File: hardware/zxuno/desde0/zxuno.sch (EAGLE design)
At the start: 98 parts, among them J1 microUSB, J12 AUX_PW, J13 SWITCH, J14 RESET_FPGA, J4 Audio, J5 EAR, J7 MINI-DIN6PTH, T1 BC846, U1 6SLX9TQG144, U2 FLASH-SPI-25XXSMD1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

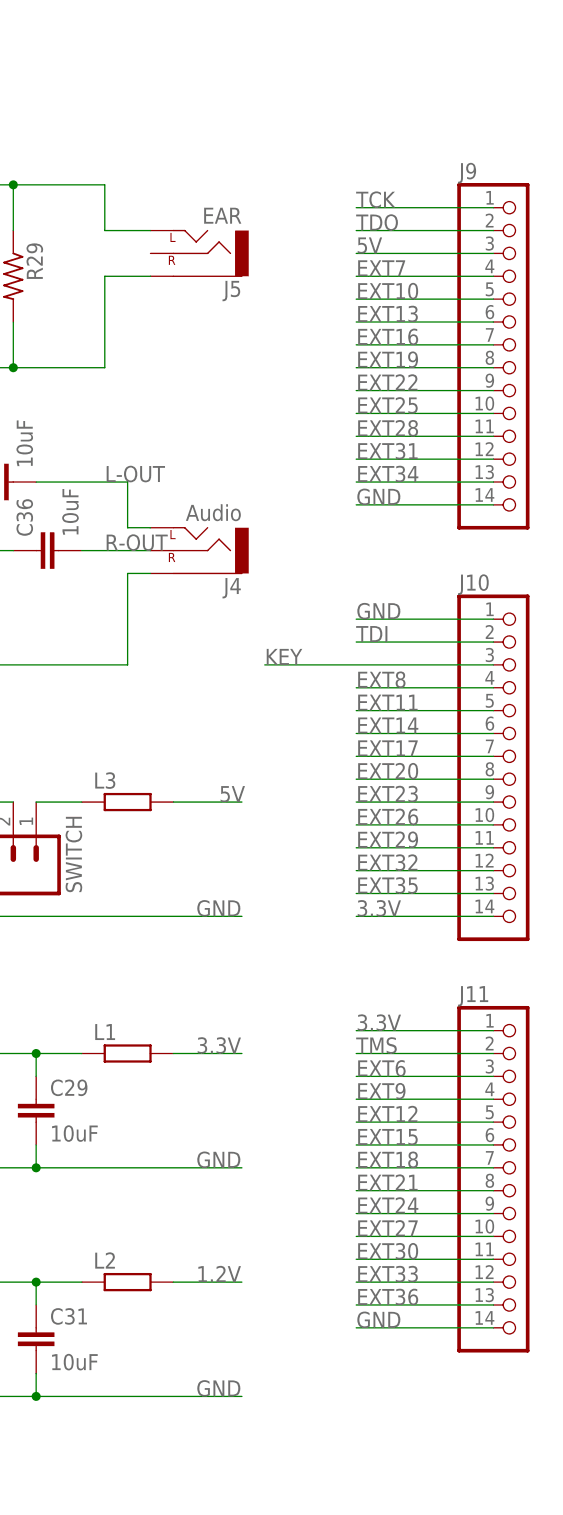
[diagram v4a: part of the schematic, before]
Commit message: 
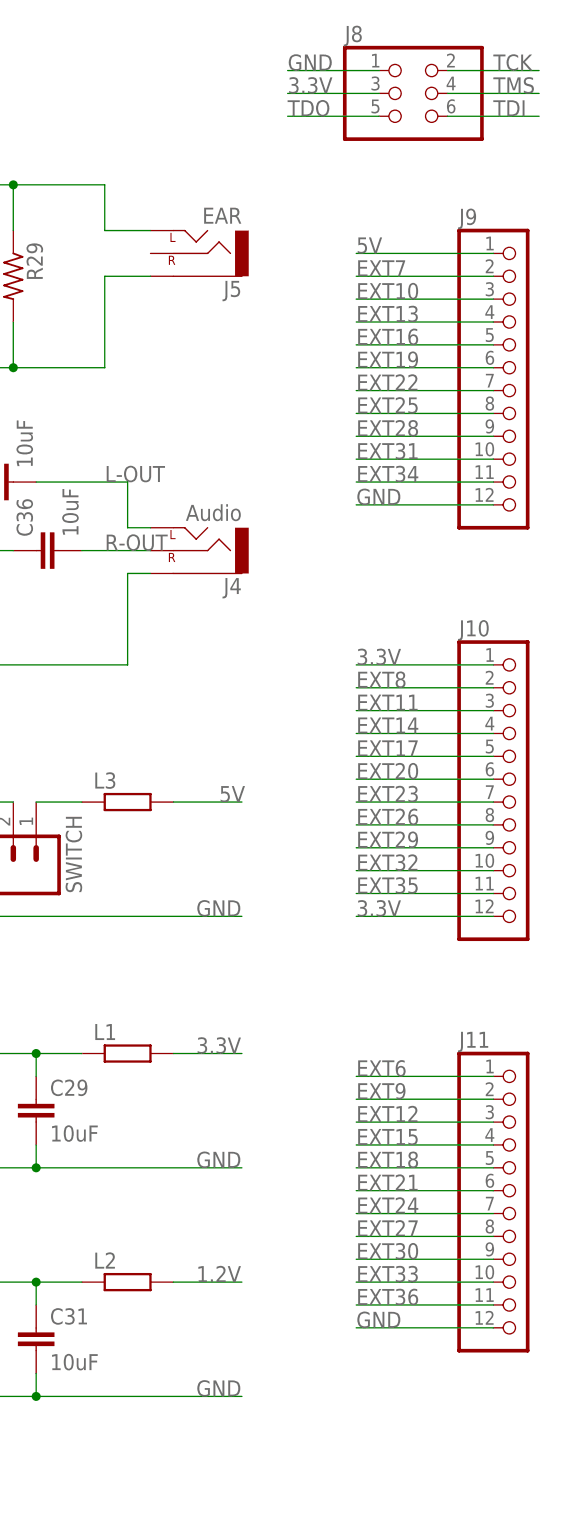
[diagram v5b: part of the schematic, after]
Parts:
- added J8: (no value), pinhead:PINHD-2X3
- J10, J11, J9: device pinhead:PINHD-1X14 -> pinhead:PINHD-1X12
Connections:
- removed net KEY: J10.3
- net 3.3V: now also J10.1, J10.12, J8.3; no longer J10.14, J11.1
- net 5V: now also J9.1; no longer J9.3
- net EXT10: now also J9.3; no longer J9.5
- net EXT11: now also J10.3; no longer J10.5
- net EXT12: now also J11.3; no longer J11.5
- net EXT13: now also J9.4; no longer J9.6
- net EXT14: now also J10.4; no longer J10.6
- net EXT15: now also J11.4; no longer J11.6
- net EXT16: now also J9.5; no longer J9.7
- net EXT17: now also J10.5; no longer J10.7
- net EXT18: now also J11.5; no longer J11.7
- net EXT19: now also J9.6; no longer J9.8
- net EXT20: now also J10.6; no longer J10.8
- net EXT21: now also J11.6; no longer J11.8
- net EXT22: now also J9.7; no longer J9.9
- net EXT23: now also J10.7; no longer J10.9
- net EXT24: now also J11.7; no longer J11.9
- net EXT25: now also J9.8; no longer J9.10
- net EXT26: now also J10.8; no longer J10.10
- net EXT27: now also J11.8; no longer J11.10
- net EXT28: now also J9.9; no longer J9.11
- net EXT29: now also J10.9; no longer J10.11
- net EXT30: now also J11.9; no longer J11.11
- net EXT31: now also J9.10; no longer J9.12
- net EXT32: now also J10.10; no longer J10.12
- net EXT33: now also J11.10; no longer J11.12
- net EXT34: now also J9.11; no longer J9.13
- net EXT35: now also J10.11; no longer J10.13
- net EXT36: now also J11.11; no longer J11.13
- net EXT6: now also J11.1; no longer J11.3
- net EXT7: now also J9.2; no longer J9.4
- net EXT8: now also J10.2; no longer J10.4
- net EXT9: now also J11.2; no longer J11.4
- net GND: now also J11.12, J8.1, J9.12; no longer J10.1, J11.14, J9.14
- net TCK: now also J8.2; no longer J9.1
- net TDI: now also J8.6; no longer J10.2
- net TDO: now also J8.5; no longer J9.2
- net TMS: now also J8.4; no longer J11.2

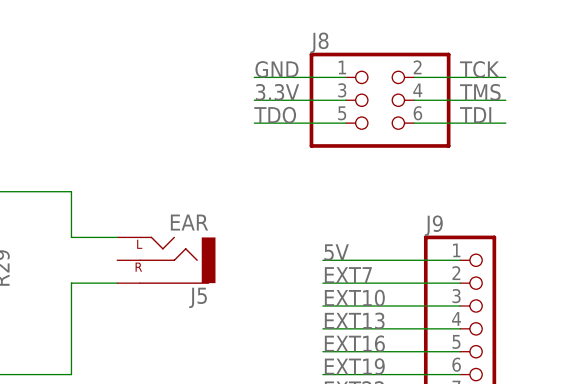
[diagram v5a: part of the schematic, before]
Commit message: 
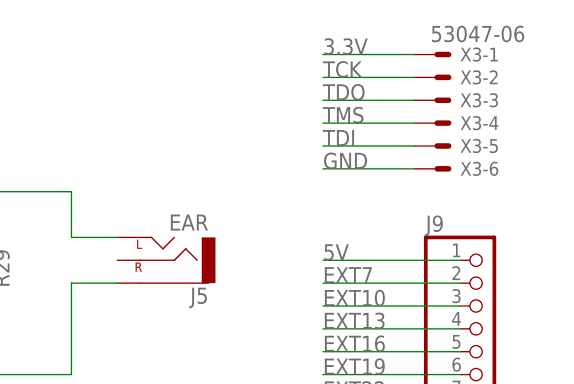
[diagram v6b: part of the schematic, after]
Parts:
- removed J8: (no value), pinhead:PINHD-2X3
- added X3: 53047-06, con-molex:53047-06
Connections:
- net 3.3V: now also X3-1.S; no longer J8.3
- net GND: now also X3-6.S; no longer J8.1
- net TCK: now also X3-2.S; no longer J8.2
- net TDI: now also X3-5.S; no longer J8.6
- net TDO: now also X3-3.S; no longer J8.5
- net TMS: now also X3-4.S; no longer J8.4
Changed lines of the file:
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@@
 <part name="GND18" library="supply1" deviceset="GND" device=""/>
 <part name="X2" library="con-molex" deviceset="53?-09" device="047"/>
-<part name="J8" library="pinhead" deviceset="PINHD-2X3" device=""/>
 <part name="J9" library="pinhead" deviceset="PINHD-1X12" device=""/>
 <part name="J10" library="pinhead" deviceset="PINHD-1X12" device=""/>
 <part name="J11" library="pinhead" deviceset="PINHD-1X12" device=""/>
+<part name="X3" library="con-molex" deviceset="53?-06" device="047"/>
 </parts>
 <sheets>
@@
 <instance part="X2" gate="-8" x="139.7" y="43.18" rot="R180"/>
 <instance part="X2" gate="-9" x="139.7" y="45.72" rot="R180"/>
-<instance part="J8" gate="A" x="266.7" y="91.44"/>
 <instance part="J9" gate="G$1" x="279.4" y="60.96"/>
 <instance part="J10" gate="G$1" x="279.4" y="15.24"/>
 <instance part="J11" gate="G$1" x="279.4" y="-30.48"/>
+<instance part="X3" gate="-1" x="274.32" y="96.52"/>
+<instance part="X3" gate="-2" x="274.32" y="93.98"/>
+<instance part="X3" gate="-3" x="274.32" y="91.44"/>
+<instance part="X3" gate="-4" x="274.32" y="88.9"/>
+<instance part="X3" gate="-5" x="274.32" y="86.36"/>
+<instance part="X3" gate="-6" x="274.32" y="83.82"/>
 </instances>
 <busses>
@@
 </segment>
 <segment>
-<wire x1="254" y1="91.44" x2="264.16" y2="91.44" width="0.1524" layer="91"/>
-<pinref part="J8" gate="A" pin="3"/>
-<label x="254" y="91.44" size="1.778" layer="95"/>
+<wire x1="261.62" y1="96.52" x2="271.78" y2="96.52" width="0.1524" layer="91"/>
+<label x="261.62" y="96.52" size="1.778" layer="95"/>
+<pinref part="X3" gate="-1" pin="S"/>
 </segment>
 </net>
@@
 </segment>
 <segment>
-<wire x1="254" y1="93.98" x2="264.16" y2="93.98" width="0.1524" layer="91"/>
-<pinref part="J8" gate="A" pin="1"/>
-<label x="254" y="93.98" size="1.778" layer="95"/>
+<wire x1="261.62" y1="83.82" x2="271.78" y2="83.82" width="0.1524" layer="91"/>
+<label x="261.62" y="83.82" size="1.778" layer="95"/>
+<pinref part="X3" gate="-6" pin="S"/>
 </segment>
 </net>
@@
 </segment>
 <segment>
-<wire x1="271.78" y1="91.44" x2="281.94" y2="91.44" width="0.1524" layer="91"/>
-<pinref part="J8" gate="A" pin="4"/>
-<label x="276.86" y="91.44" size="1.778" layer="95"/>
+<wire x1="261.62" y1="88.9" x2="271.78" y2="88.9" width="0.1524" layer="91"/>
+<label x="261.62" y="88.9" size="1.778" layer="95"/>
+<pinref part="X3" gate="-4" pin="S"/>
 </segment>
 </net>
@@
 </segment>
 <segment>
-<wire x1="271.78" y1="93.98" x2="281.94" y2="93.98" width="0.1524" layer="91"/>
-<pinref part="J8" gate="A" pin="2"/>
-<label x="276.86" y="93.98" size="1.778" layer="95"/>
+<wire x1="261.62" y1="93.98" x2="271.78" y2="93.98" width="0.1524" layer="91"/>
+<label x="261.62" y="93.98" size="1.778" layer="95"/>
+<pinref part="X3" gate="-2" pin="S"/>
 </segment>
 </net>
@@
 </segment>
 <segment>
-<wire x1="254" y1="88.9" x2="264.16" y2="88.9" width="0.1524" layer="91"/>
-<pinref part="J8" gate="A" pin="5"/>
-<label x="254" y="88.9" size="1.778" layer="95"/>
+<wire x1="261.62" y1="91.44" x2="271.78" y2="91.44" width="0.1524" layer="91"/>
+<label x="261.62" y="91.44" size="1.778" layer="95"/>
+<pinref part="X3" gate="-3" pin="S"/>
 </segment>
 </net>
@@
 </segment>
 <segment>
-<wire x1="271.78" y1="88.9" x2="281.94" y2="88.9" width="0.1524" layer="91"/>
-<pinref part="J8" gate="A" pin="6"/>
-<label x="276.86" y="88.9" size="1.778" layer="95"/>
-</segment>
-</net>
+<wire x1="261.62" y1="86.36" x2="271.78" y2="86.36" width="0.1524" layer="91"/>
+<label x="261.62" y="86.36" size="1.778" layer="95"/>
+<pinref part="X3" gate="-5" pin="S"/>
+</segment>
+</net>

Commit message: 
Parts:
- removed J12: AUX_PW, SparkFun-Connectors:M02POLAR
- removed J13: SWITCH, SparkFun-Connectors:M02POLAR
- removed J14: RESET_FPGA, SparkFun-Connectors:M02POLAR
- added JP1, JP2, JP3: (no value), pinhead:PINHD-1X2
- X2: value 53047-09 -> 53048-09; device con-molex:53047-09 -> con-molex:53048-09
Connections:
- net GND: now also JP1.1, JP3.1; no longer J12.1, J14.1
- net N$12: now also JP2.2, JP3.2; no longer J12.2, J13.2
- net N$13: now also JP2.1; no longer J13.1
- net N$5: now also JP1.2; no longer J14.2
- net TCK: now also X3-4.S; no longer X3-2.S
- net TDO: now also X3-2.S; no longer X3-3.S
- net TMS: now also X3-3.S; no longer X3-4.S

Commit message: 
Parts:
- C32: device rcl:CPOL-US153CLV-0807 -> rcl:CPOL-US153CLV-0605
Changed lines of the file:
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@@
 <part name="C1" library="rcl" deviceset="C-EU" device="C0805" value="7.5pF"/>
 <part name="GND12" library="supply1" deviceset="GND" device=""/>
-<part name="C32" library="rcl" deviceset="CPOL-US" device="153CLV-0807" value="220uF"/>
+<part name="C32" library="rcl" deviceset="CPOL-US" device="153CLV-0605" value="220uF"/>
 <part name="GND13" library="supply1" deviceset="GND" device=""/>
 <part name="R6" library="rcl" deviceset="R-US_" device="M0805" value="510"/>
